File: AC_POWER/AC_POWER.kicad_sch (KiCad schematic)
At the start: 7 parts, among them J1 5.5 OD x 2.1 ID

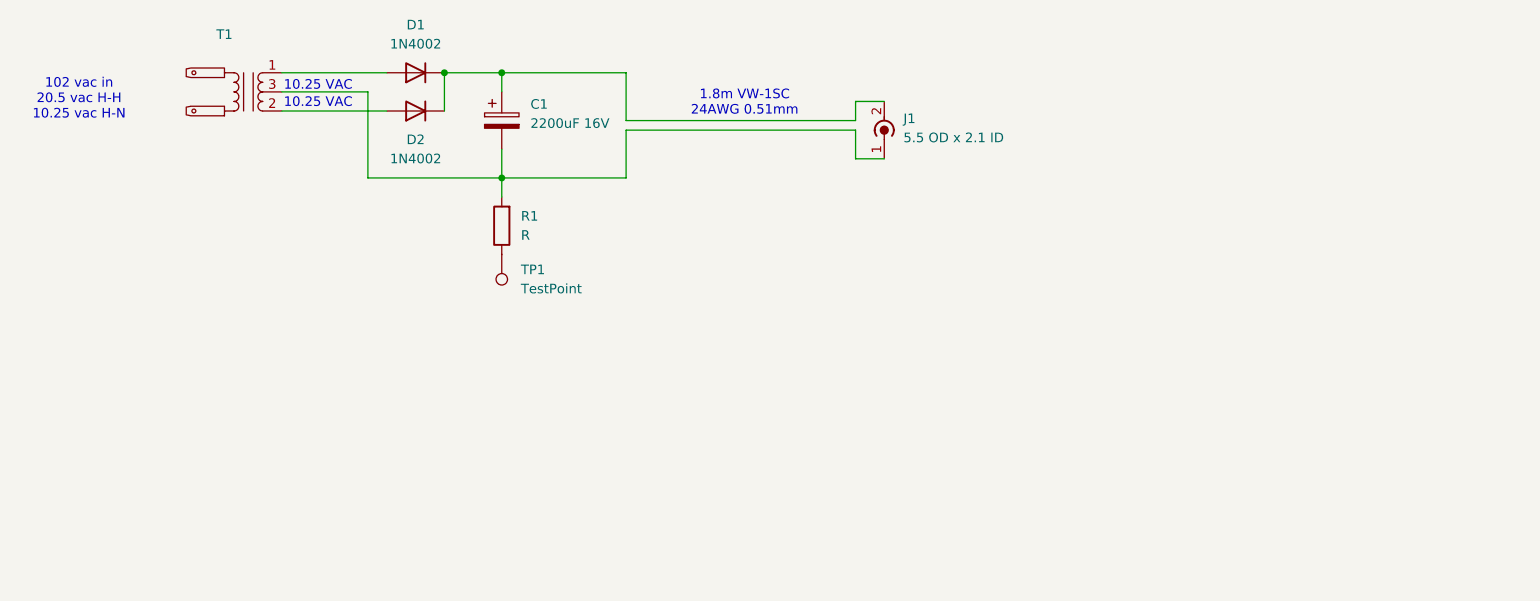
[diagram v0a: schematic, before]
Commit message: add solder mask to PCB and clarify notes on schematic
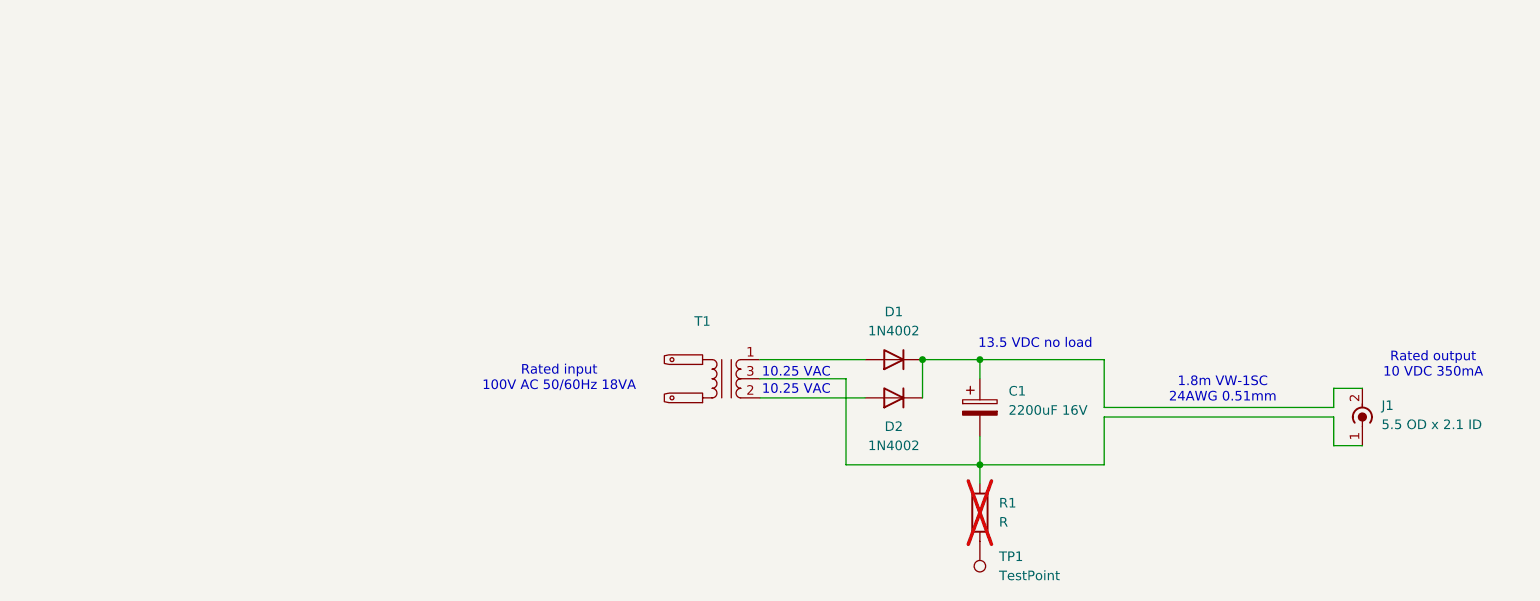
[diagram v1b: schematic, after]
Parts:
- R1: now not fitted; now left out of the parts list
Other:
- note added: "13.5 VDC no load"
- note added: "Rated input 100V AC 50/60Hz 18VA"
- note added: "Rated output 10 VDC 350mA"
- note removed: "102 vac in 20.5 vac H-H 10.25 vac H-N"
- moved on the sheet: C1, D1, D2, J1, T1, TP1
